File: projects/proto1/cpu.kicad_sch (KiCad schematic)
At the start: 20 parts, among them U1 MC68030R, U2 MC68882FN

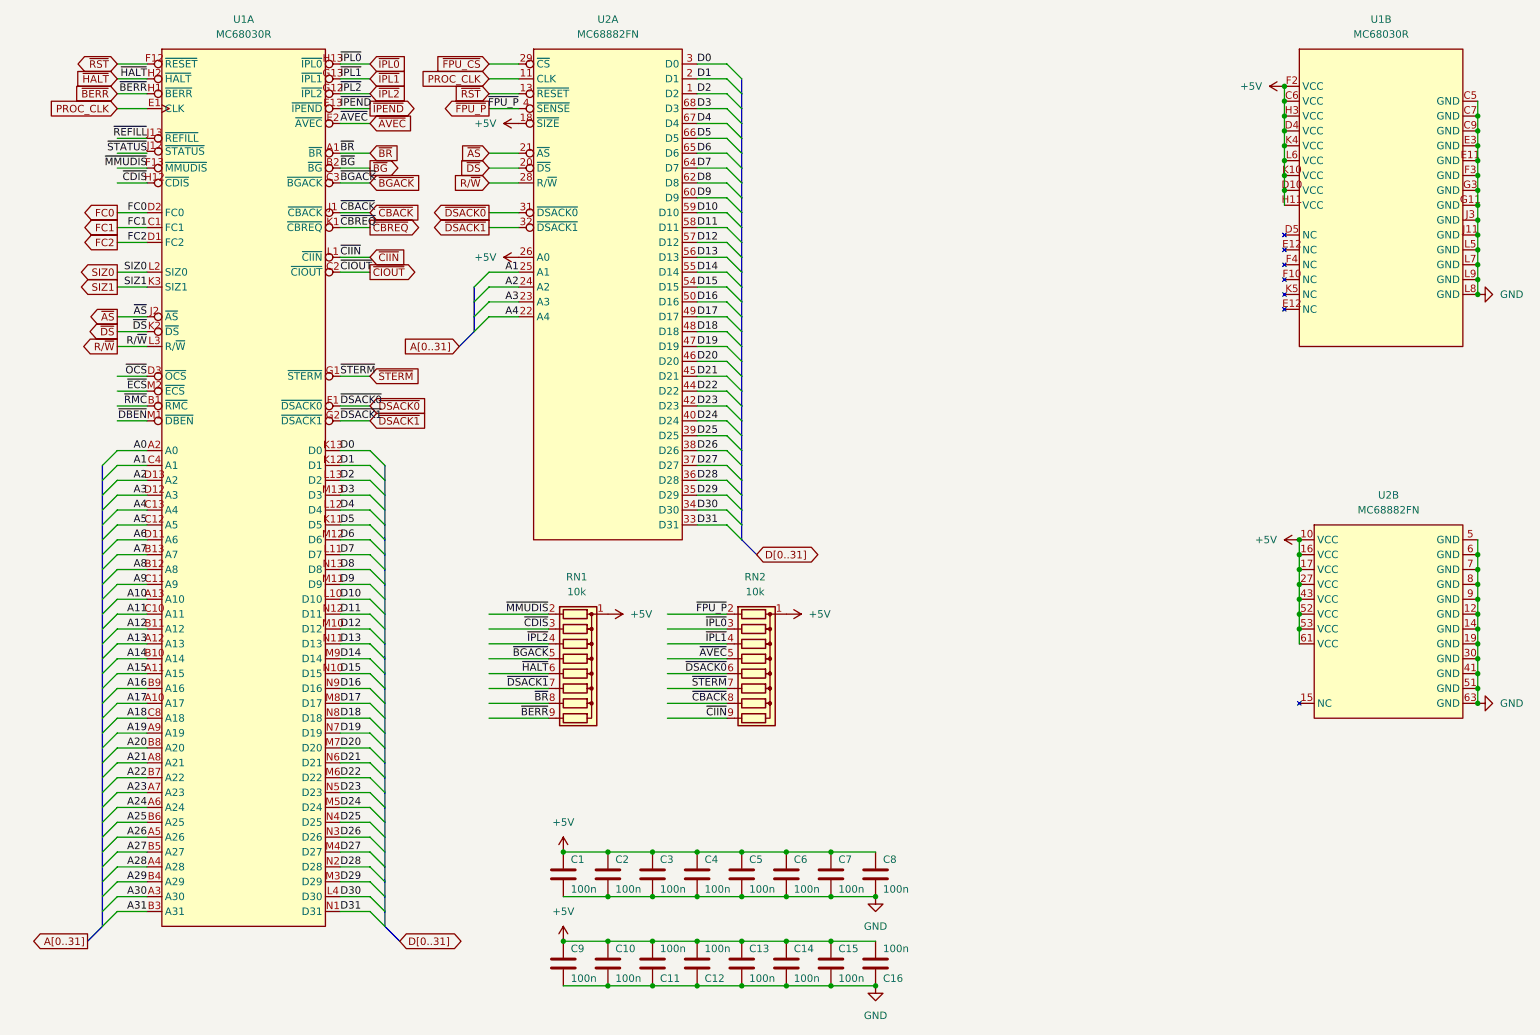
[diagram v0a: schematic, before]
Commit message: Renamed CMC to SCU, changed verification method to cocotb, and modified pcb schematic
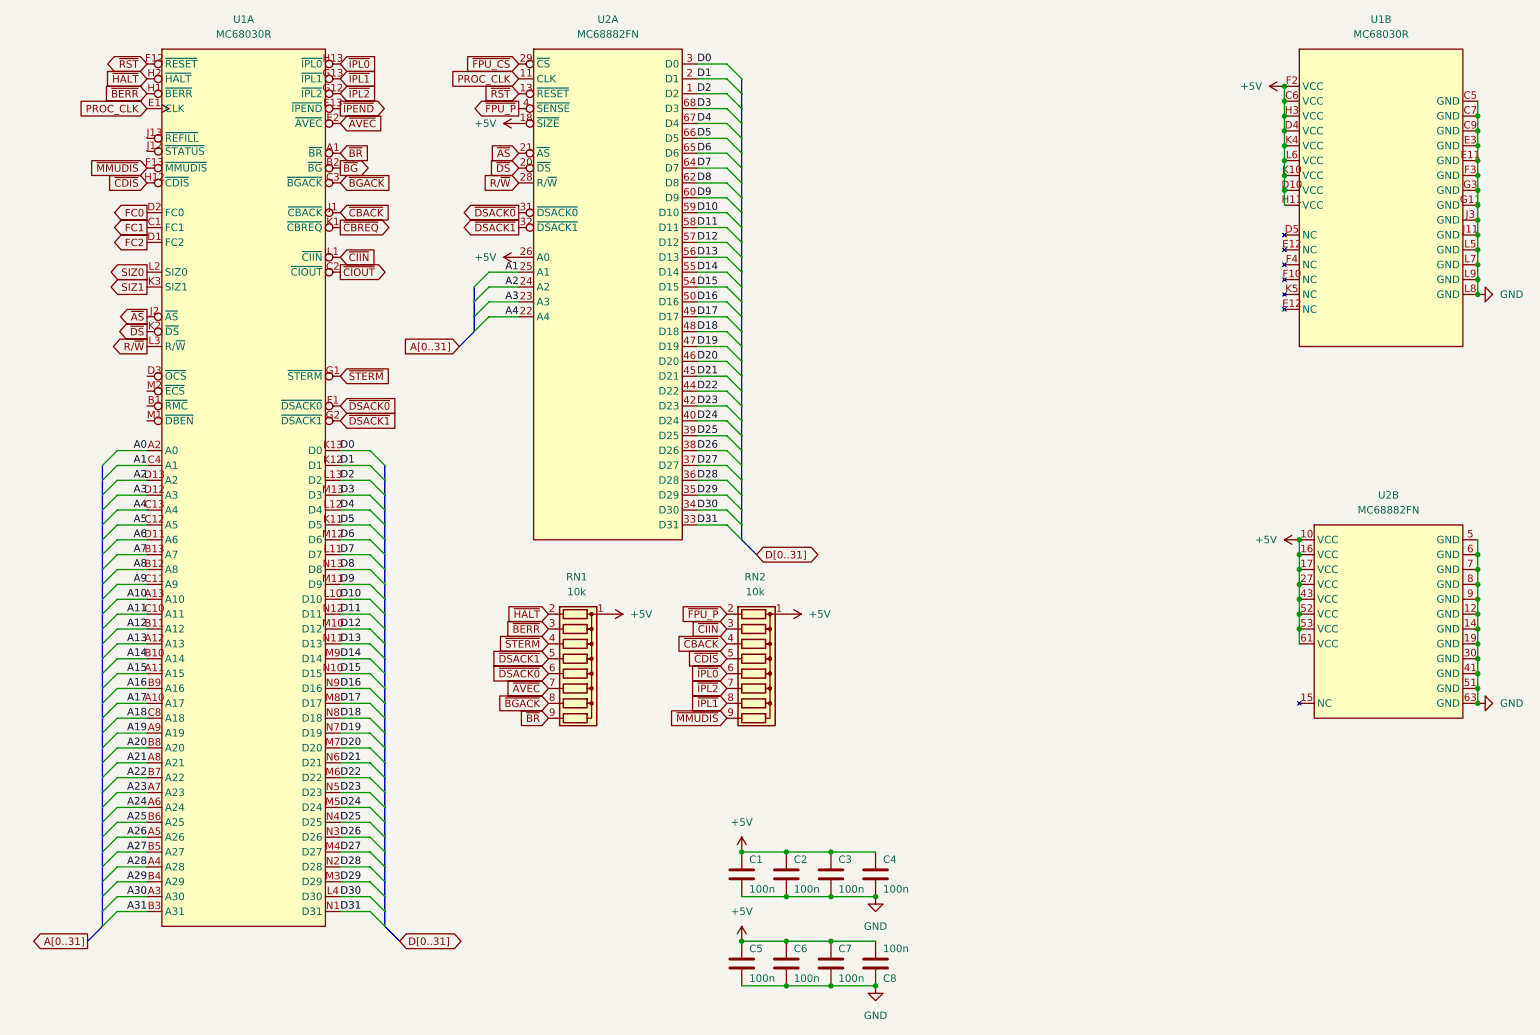
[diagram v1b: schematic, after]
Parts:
- removed C1, C10, C11, C12, C2, C3, C4, C9: 100n, Capacitor_THT:C_Disc_D4.3mm_W1.9mm_P5.00mm, symbol Device:C
- renumbered C5 to C1, C6 to C2, C7 to C3, C8 to C4, C13 to C5, C14 to C6, C15 to C7, C16 to C8
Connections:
- net ~{AVEC}: now also RN1.7 (R6); no longer RN2.5 (R4)
- net ~{BERR}: now also RN1.3 (R2); no longer RN1.9 (R8)
- net ~{BGACK}: now also RN1.8 (R7); no longer RN1.5 (R4)
- net ~{BR}: now also RN1.9 (R8); no longer RN1.8 (R7)
- net ~{CBACK}: now also RN2.4 (R3); no longer RN2.8 (R7)
- net ~{CDIS}: now also RN2.5 (R4); no longer RN1.3 (R2)
- net ~{CIIN}: now also RN2.3 (R2); no longer RN2.9 (R8)
- net ~{DSACK0}: now also RN1.6 (R5); no longer RN2.6 (R5)
- net ~{DSACK1}: now also RN1.5 (R4); no longer RN1.7 (R6)
- net ~{HALT}: now also RN1.2 (R1); no longer RN1.6 (R5)
- net ~{IPL0}: now also RN2.6 (R5); no longer RN2.3 (R2)
- net ~{IPL1}: now also RN2.8 (R7); no longer RN2.4 (R3)
- net ~{IPL2}: now also RN2.7 (R6); no longer RN1.4 (R3)
- net ~{MMUDIS}: now also RN2.9 (R8); no longer RN1.2 (R1)
- net ~{STERM}: now also RN1.4 (R3); no longer RN2.7 (R6)
- net ~{DBEN}: no longer names the net of U1.M1 (~{DBEN})
- net ~{ECS}: no longer names the net of U1.M2 (~{ECS})
- net ~{OCS}: no longer names the net of U1.D3 (~{OCS})
- net ~{REFILL}: no longer names the net of U1.J13 (~{REFILL})
- net ~{RMC}: no longer names the net of U1.B1 (~{RMC})
